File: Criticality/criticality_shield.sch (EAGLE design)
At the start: 20 parts

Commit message: some small improvements
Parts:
- renumbered SV2 to D8-13
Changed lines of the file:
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@@
 <setting verticaltext="up"/>
 </settings>
-<grid distance="0.1" unitdist="inch" unit="inch" style="lines" multiple="1" display="yes" altdistance="0.1" altunitdist="inch" altunit="inch"/>
+<grid distance="0.1" unitdist="inch" unit="inch" style="lines" multiple="1" display="no" altdistance="0.01" altunitdist="inch" altunit="inch"/>
 <layers>
 <layer number="1" name="Top" color="4" fill="1" visible="no" active="no"/>
@@
 <part name="GND2" library="supply1" deviceset="GND" device=""/>
 <part name="D0-7" library="con-lstb" deviceset="MA08-1" device=""/>
-<part name="SV2" library="con-lstb" deviceset="MA08-1" device=""/>
+<part name="D8-13" library="con-lstb" deviceset="MA08-1" device=""/>
 <part name="R9" library="SparkFun-Passives" deviceset="RESISTOR" device="1206" value="100"/>
 <part name="R10" library="SparkFun-Passives" deviceset="RESISTOR" device="1206" value="100"/>
@@
 <instance part="GND2" gate="1" x="-50.8" y="119.38"/>
 <instance part="D0-7" gate="1" x="-88.9" y="111.76" rot="R90"/>
-<instance part="SV2" gate="1" x="-88.9" y="48.26" rot="R90"/>
+<instance part="D8-13" gate="1" x="-88.9" y="48.26" rot="R90"/>
 <instance part="R9" gate="G$1" x="-66.04" y="101.6"/>
 <instance part="R10" gate="G$1" x="-66.04" y="93.98"/>
@@
 <segment>
 <pinref part="R9" gate="G$1" pin="1"/>
-<wire x1="-76.2" y1="101.6" x2="-71.12" y2="101.6" width="0.1524" layer="91"/>
-<junction x="-71.12" y="101.6"/>
-<pinref part="SV2" gate="1" pin="3"/>
+<pinref part="D8-13" gate="1" pin="3"/>
 <wire x1="-86.36" y1="55.88" x2="-71.12" y2="101.6" width="0.1524" layer="91"/>
 <junction x="-86.36" y="55.88"/>
+<junction x="-71.12" y="101.6"/>
 </segment>
 </net>
@@
 <segment>
 <pinref part="R10" gate="G$1" pin="1"/>
-<wire x1="-71.12" y1="93.98" x2="-76.2" y2="93.98" width="0.1524" layer="91"/>
-<junction x="-71.12" y="93.98"/>
-<pinref part="SV2" gate="1" pin="4"/>
+<pinref part="D8-13" gate="1" pin="4"/>
 <wire x1="-88.9" y1="55.88" x2="-71.12" y2="93.98" width="0.1524" layer="91"/>
 <junction x="-88.9" y="55.88"/>
+<junction x="-71.12" y="93.98"/>
 </segment>
 </net>
@@
 <wire x1="-76.2" y1="86.36" x2="-71.12" y2="86.36" width="0.1524" layer="91"/>
 <junction x="-71.12" y="86.36"/>
-<pinref part="SV2" gate="1" pin="5"/>
+<pinref part="D8-13" gate="1" pin="5"/>
 <wire x1="-91.44" y1="55.88" x2="-71.12" y2="86.36" width="0.1524" layer="91"/>
 <junction x="-91.44" y="55.88"/>
@@
 <wire x1="-76.2" y1="78.74" x2="-71.12" y2="78.74" width="0.1524" layer="91"/>
 <junction x="-71.12" y="78.74"/>
-<pinref part="SV2" gate="1" pin="6"/>
+<pinref part="D8-13" gate="1" pin="6"/>
 <wire x1="-93.98" y1="55.88" x2="-71.12" y2="78.74" width="0.1524" layer="91"/>
 <junction x="-93.98" y="55.88"/>
@@
 <wire x1="-76.2" y1="71.12" x2="-71.12" y2="71.12" width="0.1524" layer="91"/>
 <junction x="-71.12" y="71.12"/>
-<pinref part="SV2" gate="1" pin="7"/>
+<pinref part="D8-13" gate="1" pin="7"/>
 <wire x1="-96.52" y1="55.88" x2="-71.12" y2="71.12" width="0.1524" layer="91"/>
 <junction x="-96.52" y="55.88"/>
@@
 <net name="N$15" class="0">
 <segment>
-<pinref part="SV2" gate="1" pin="1"/>
+<pinref part="D8-13" gate="1" pin="1"/>
 <pinref part="R7" gate="G$1" pin="1"/>
 <wire x1="-81.28" y1="55.88" x2="-71.12" y2="116.84" width="0.1524" layer="91"/>
@@
 <net name="N$16" class="0">
 <segment>
-<pinref part="SV2" gate="1" pin="2"/>
+<pinref part="D8-13" gate="1" pin="2"/>
 <pinref part="R8" gate="G$1" pin="1"/>
 <wire x1="-83.82" y1="55.88" x2="-71.12" y2="109.22" width="0.1524" layer="91"/>
@@
 <net name="N$17" class="0">
 <segment>
-<pinref part="SV2" gate="1" pin="8"/>
+<pinref part="D8-13" gate="1" pin="8"/>
 <pinref part="R14" gate="G$1" pin="1"/>
 <wire x1="-99.06" y1="55.88" x2="-71.12" y2="63.5" width="0.1524" layer="91"/>

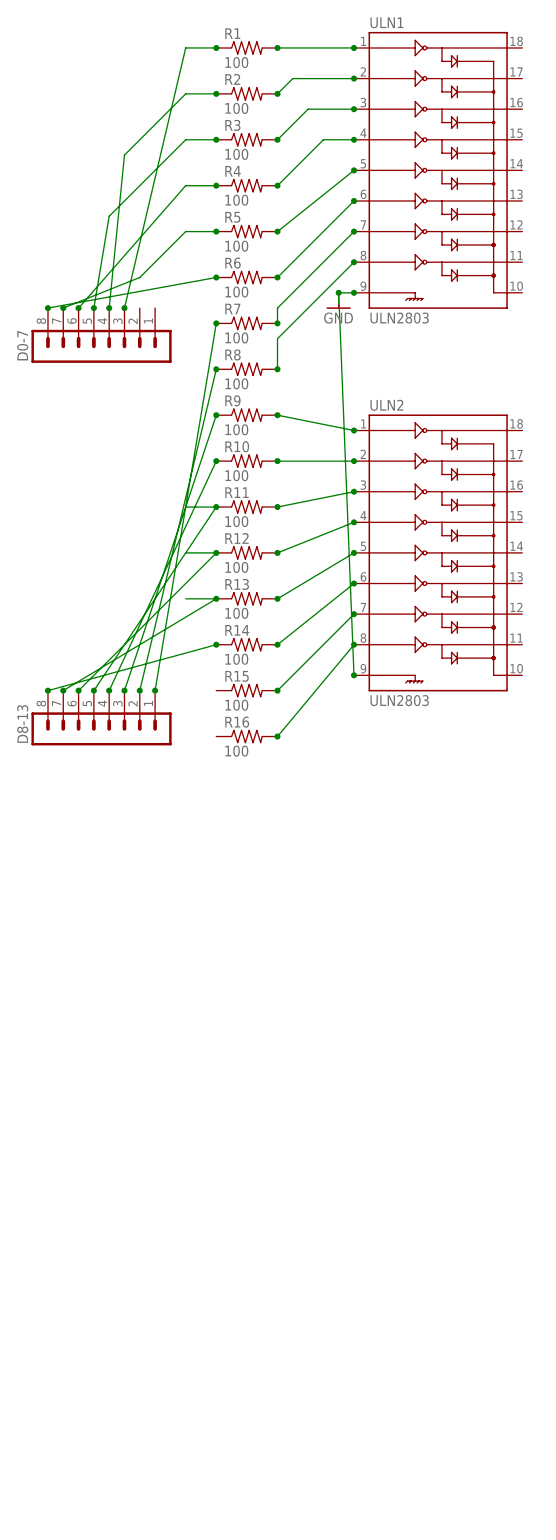
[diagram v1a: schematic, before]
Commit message: added layers to "criticality"
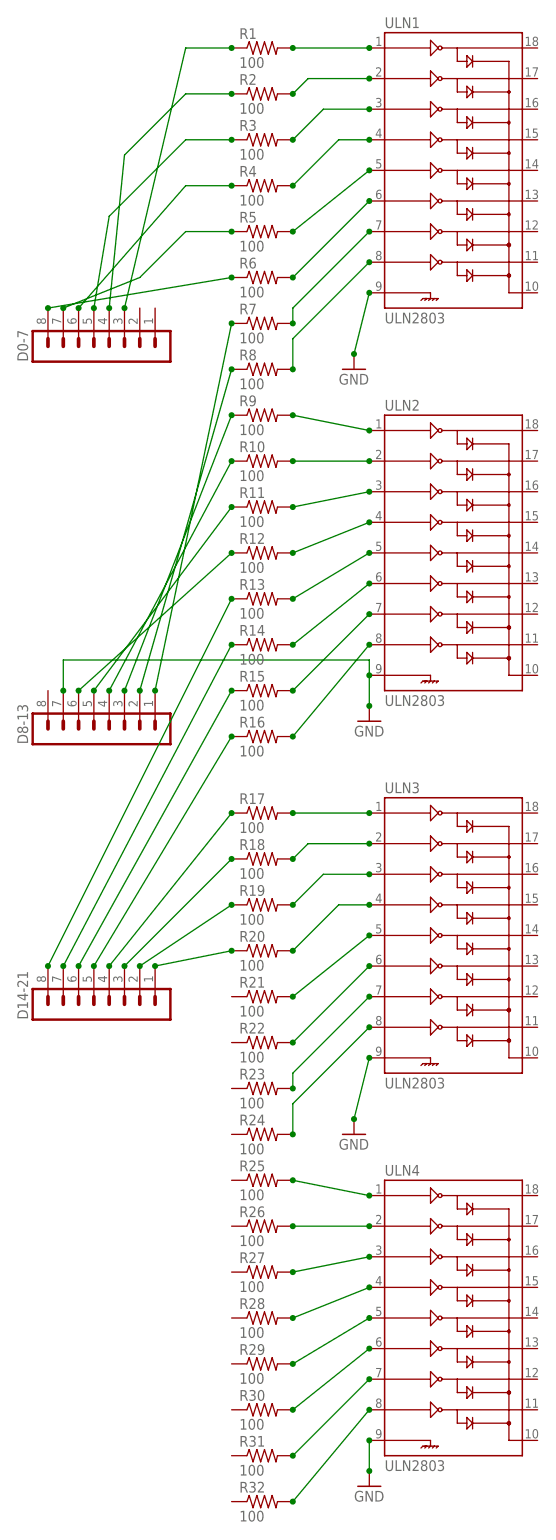
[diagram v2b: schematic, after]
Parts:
- added D14-21: (no value), con-lstb:MA08-1
- added R17, R18, R19, R20, R21, R22, R23, R24, R25, R26, R27, R28, R29, R30, R31, R32: 100, SparkFun-Passives:RESISTOR1206
- added ULN3, ULN4: ULN2803, SparkFun-PowerIC:ULN2803DIP
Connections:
- new net N$31: D14-21.6, R15.1
- new net N$32: D14-21.5, R16.1
- new net N$33: R21.2, ULN3.5
- new net N$34: R22.2, ULN3.6
- new net N$35: R23.2, ULN3.7
- new net N$36: R24.2, ULN3.8
- new net N$37: D14-21.7, R14.1
- new net N$38: D14-21.2, R19.1
- new net N$39: D14-21.1, R20.1
- new net N$40: D14-21.3, R18.1
- new net N$43: R18.2, ULN3.2
- new net N$44: R19.2, ULN3.3
- new net N$45: R20.2, ULN3.4
- new net N$46: R17.2, ULN3.1
- new net N$53: R25.2, ULN4.1
- new net N$54: R26.2, ULN4.2
- new net N$55: R27.2, ULN4.3
- new net N$56: R28.2, ULN4.4
- new net N$57: R29.2, ULN4.5
- new net N$58: R30.2, ULN4.6
- new net N$59: R31.2, ULN4.7
- new net N$60: R32.2, ULN4.8
- net GND: now also D8-13.7, ULN3.9, ULN4.9
- net N$17: now also D14-21.8, R13.1; no longer D8-13.8, R14.1
- net N$23: now also D14-21.4, R17.1; no longer D8-13.7, R13.1
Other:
- moved on the sheet: R1, R10, R11, R12, R13, R14, R15, R16, R2, R3, R4, R5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

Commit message: rearranged, all parts connected
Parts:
- added D22-36_EVEN, D23-37-ODD, D38-52-EVEN, D39-53-ODD: (no value), con-lstb:MA09-1
- added R33, R34, R35, R36, R37, R38, R39, R40, R41, R42, R43, R44, R45, R46, R47, R48: 100, SparkFun-Passives:RESISTOR1206
- added ULN5, ULN6: ULN2803, SparkFun-PowerIC:ULN2803DIP
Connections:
- removed net N$17 (its old number): D14-21.8, R13.1
- new net +5V: D22-36_EVEN.9, D23-37-ODD.9, ULN1.10, ULN2.10, ULN3.10, ULN4.10, ULN5.10, ULN6.10
- new net N$20: D14-21.1, R13.1
- new net N$21: D14-21.2, R14.1
- new net N$22: D14-21.3, R15.1
- new net N$41: D22-36_EVEN.6, R23.1
- new net N$42: D22-36_EVEN.5, R24.1
- new net N$47: D22-36_EVEN.4, R25.1
- new net N$48: D22-36_EVEN.3, R26.1
- new net N$49: D22-36_EVEN.2, R27.1
- new net N$50: D22-36_EVEN.1, R28.1
- new net N$51: D23-37-ODD.8, R29.1
- new net N$52: D23-37-ODD.7, R30.1
- new net N$61: D23-37-ODD.6, R31.1
- new net N$62: D23-37-ODD.5, R32.1
- new net N$63: D23-37-ODD.4, R33.1
- new net N$64: R33.2, ULN5.1
- new net N$65: R34.2, ULN5.2
- new net N$68: R35.2, ULN5.3
- new net N$69: R36.2, ULN5.4
- new net N$70: R37.2, ULN5.5
- new net N$71: R38.2, ULN5.6
- new net N$72: R39.2, ULN5.7
- new net N$73: R40.2, ULN5.8
- new net N$74: R41.2, ULN6.1
- new net N$75: R42.2, ULN6.2
- new net N$76: R43.2, ULN6.3
- new net N$77: R44.2, ULN6.4
- new net N$78: R45.2, ULN6.5
- new net N$79: R46.2, ULN6.6
- new net N$80: R47.2, ULN6.7
- new net N$81: R48.2, ULN6.8
- new net N$82: D23-37-ODD.3, R34.1
- new net N$83: D23-37-ODD.2, R35.1
- new net N$84: D23-37-ODD.1, R36.1
- new net N$85: D38-52-EVEN.9, R37.1
- new net N$86: D38-52-EVEN.8, R38.1
- new net N$87: D38-52-EVEN.7, R39.1
- new net N$88: D38-52-EVEN.6, R40.1
- new net N$89: D38-52-EVEN.5, R41.1
- new net N$90: D38-52-EVEN.4, R42.1
- new net N$91: D38-52-EVEN.3, R43.1
- new net N$92: D38-52-EVEN.2, R44.1
- new net N$93: D39-53-ODD.9, R45.1
- new net N$94: D39-53-ODD.8, R46.1
- new net N$95: D39-53-ODD.7, R47.1
- new net N$96: D39-53-ODD.6, R48.1
- net GND: now also D38-52-EVEN.1, D39-53-ODD.1, ULN5.9, ULN6.9
- net N$23: now also R16.1; no longer R17.1
- net N$31: now also D14-21.5, R17.1; no longer D14-21.6, R15.1
- net N$32: now also D14-21.6, R18.1; no longer D14-21.5, R16.1
- net N$37: now also R19.1; no longer R14.1
- net N$38: now also D14-21.8, R20.1; no longer D14-21.2, R19.1
- net N$39: now also D22-36_EVEN.8, R21.1; no longer D14-21.1, R20.1
- net N$40: now also D22-36_EVEN.7, R22.1; no longer D14-21.3, R18.1
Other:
- note added: "10"
- note added: "11"
- note added: "12"
- note added: "13"
- note added: "14"
- note added: "15"
- note added: "16"
- note added: "17"
- note added: "18"
- note added: "19"
- note added: "2"
- note added: "20"
- note added: "21"
- note added: "22"
- note added: "23"
- note added: "24"
- note added: "25"
- note added: "26"
- note added: "27"
- note added: "28"
- note added: "29"
- note added: "3"
- note added: "30"
- note added: "31"
- note added: "32"
- note added: "33"
- note added: "34"
- note added: "35"
- note added: "36"
- note added: "37"
- note added: "38"
- note added: "39"
- note added: "4"
- note added: "40"
- note added: "41"
- note added: "42"
- note added: "43"
- note added: "44"
- note added: "45"
- note added: "46"
- note added: "47"
- note added: "48"
- note added: "49"
- note added: "5"
- note added: "50"
- note added: "51"
- note added: "52"
- note added: "53"
- note added: "6"
- note added: "7"
- note added: "8"
- note added: "9"
- moved on the sheet: D0-7, D14-21, D8-13

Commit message: clean up, almost finished
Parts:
- removed R1, R10, R11, R12, R13, R14, R15, R16, R17, R18, R19, R2, R20, R21, R22, R23, R24, R25, R26, R27, R28, R29, R3, R30, R31, R32, R33, R34, R35, R36, R37, R38, R39, R4, R40, R41, R42, R43, R44, R45, R46, R47, R48, R5, R6, R7, R8, R9: 100, SparkFun-Passives:RESISTOR1206
- added JP1: (no value), pinhead:PINHD-2X8
- added R-ARRAY-1, R-ARRAY-2, R-ARRAY-3, R-ARRAY-4, R-ARRAY-5, R-ARRAY-6, R-ARRAY-8: (no value), ic-package:DIL16
- added ULN7: ULN2803, SparkFun-PowerIC:ULN2803DIP
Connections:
- new net N$100: R-ARRAY-6.13, ULN6.4
- new net N$101: R-ARRAY-6.12, ULN6.5
- new net N$102: R-ARRAY-6.11, ULN6.6
- new net N$103: R-ARRAY-6.10, ULN6.7
- new net N$104: R-ARRAY-6.9, ULN6.8
- new net N$97: R-ARRAY-6.16, ULN6.1
- new net N$98: R-ARRAY-6.15, ULN6.2
- new net N$99: R-ARRAY-6.14, ULN6.3
- net +5V: now also ULN7.10
- net GND: now also ULN7.9
- net N$1: now also R-ARRAY-8.1; no longer R1.1
- net N$10: now also R-ARRAY-8.15, ULN1.2; no longer R1.2, ULN1.1
- net N$11: now also R-ARRAY-8.14, ULN1.3; no longer R5.2, ULN1.5
- net N$12: now also R-ARRAY-8.13, ULN1.4; no longer R6.2, ULN1.6
- net N$13: now also D8-13.3, R-ARRAY-1.3; no longer R7.2, ULN1.7
- net N$14: now also D8-13.4, R-ARRAY-1.4; no longer R8.2, ULN1.8
- net N$15: now also D8-13.5, R-ARRAY-1.5; no longer D8-13.3, R9.1
- net N$16: now also D8-13.6, R-ARRAY-1.6; no longer D8-13.4, R10.1
- net N$17: now also R-ARRAY-1.16, ULN2.1; no longer D8-13.5, R11.1
- net N$18: now also R-ARRAY-1.15, ULN2.2; no longer R9.2, ULN2.1
- net N$19: now also R-ARRAY-1.14, ULN2.3; no longer D8-13.6, R12.1
- net N$2: now also D0-7.4, R-ARRAY-8.2; no longer D0-7.7, R5.1
- net N$20: now also R-ARRAY-2.1; no longer R13.1
- net N$21: now also R-ARRAY-2.2; no longer R14.1
- net N$22: now also R-ARRAY-2.3; no longer R15.1
- net N$23: now also R-ARRAY-2.4; no longer R16.1
- net N$24: now also R-ARRAY-1.13, ULN2.4; no longer R10.2, ULN2.2
- net N$25: now also R-ARRAY-1.12, ULN2.5; no longer R11.2, ULN2.3
- net N$26: now also R-ARRAY-1.11, ULN2.6; no longer R12.2, ULN2.4
- net N$27: now also D14-21.5, R-ARRAY-2.5; no longer R13.2, ULN2.5
- net N$28: now also D14-21.6, R-ARRAY-2.6; no longer R14.2, ULN2.6
- net N$29: now also D14-21.7, R-ARRAY-2.7; no longer R15.2, ULN2.7
- net N$3: now also D0-7.5, R-ARRAY-8.3; no longer D0-7.8, R6.1
- net N$30: now also D14-21.8, R-ARRAY-2.8; no longer R16.2, ULN2.8
- net N$31: now also R-ARRAY-2.16, ULN3.1; no longer D14-21.5, R17.1
- net N$32: now also R-ARRAY-2.15, ULN3.2; no longer D14-21.6, R18.1
- net N$33: now also R-ARRAY-2.14, ULN3.3; no longer R21.2, ULN3.5
- net N$34: now also R-ARRAY-2.13, ULN3.4; no longer R22.2, ULN3.6
- net N$35: now also D22-36_EVEN.1, R-ARRAY-3.1; no longer R23.2, ULN3.7
- net N$36: now also D22-36_EVEN.2, R-ARRAY-3.2; no longer R24.2, ULN3.8
- net N$37: now also R-ARRAY-2.12, ULN3.5; no longer D14-21.7, R19.1
- net N$38: now also R-ARRAY-2.11, ULN3.6; no longer D14-21.8, R20.1
- net N$39: now also D22-36_EVEN.3, R-ARRAY-3.3; no longer D22-36_EVEN.8, R21.1
- net N$4: now also R-ARRAY-8.4; no longer R4.1
- net N$40: now also D22-36_EVEN.4, R-ARRAY-3.4; no longer D22-36_EVEN.7, R22.1
- net N$41: now also D22-36_EVEN.5, R-ARRAY-3.5; no longer D22-36_EVEN.6, R23.1
- net N$42: now also D22-36_EVEN.6, R-ARRAY-3.6; no longer D22-36_EVEN.5, R24.1
- net N$43: now also R-ARRAY-2.10, ULN3.7; no longer R18.2, ULN3.2
- net N$44: now also R-ARRAY-2.9, ULN3.8; no longer R19.2, ULN3.3
- net N$45: now also D22-36_EVEN.7, R-ARRAY-3.7; no longer R20.2, ULN3.4
- net N$46: now also D22-36_EVEN.8, R-ARRAY-3.8; no longer R17.2, ULN3.1
- net N$47: now also R-ARRAY-3.16, ULN4.1; no longer D22-36_EVEN.4, R25.1
- net N$48: now also R-ARRAY-3.15, ULN4.2; no longer D22-36_EVEN.3, R26.1
- net N$49: now also R-ARRAY-3.14, ULN4.3; no longer D22-36_EVEN.2, R27.1
- net N$5: now also R-ARRAY-1.1; no longer R7.1
- net N$50: now also R-ARRAY-3.13, ULN4.4; no longer D22-36_EVEN.1, R28.1
- net N$51: now also R-ARRAY-4.1; no longer R29.1
- net N$52: now also R-ARRAY-4.2; no longer R30.1
- net N$53: now also R-ARRAY-3.12, ULN4.5; no longer R25.2, ULN4.1
- net N$54: now also R-ARRAY-3.11, ULN4.6; no longer R26.2, ULN4.2
- net N$55: now also R-ARRAY-3.10, ULN4.7; no longer R27.2, ULN4.3
- net N$56: now also R-ARRAY-3.9, ULN4.8; no longer R28.2, ULN4.4
- net N$57: now also D23-37-ODD.6, R-ARRAY-4.3; no longer R29.2, ULN4.5
- net N$58: now also D23-37-ODD.5, R-ARRAY-4.4; no longer R30.2, ULN4.6
- net N$59: now also D23-37-ODD.4, R-ARRAY-4.5; no longer R31.2, ULN4.7
- net N$6: now also R-ARRAY-1.2; no longer R8.1
- net N$60: now also D23-37-ODD.3, R-ARRAY-4.6; no longer R32.2, ULN4.8
- net N$61: now also D23-37-ODD.2, R-ARRAY-4.7; no longer D23-37-ODD.6, R31.1
- net N$62: now also D23-37-ODD.1, R-ARRAY-4.8; no longer D23-37-ODD.5, R32.1
- net N$63: now also R-ARRAY-4.16, ULN7.1; no longer D23-37-ODD.4, R33.1
- net N$64: now also R-ARRAY-4.15, ULN7.2; no longer R33.2, ULN5.1
- net N$65: now also R-ARRAY-4.14, ULN7.3; no longer R34.2, ULN5.2
- net N$66: now also R-ARRAY-8.12, ULN1.5; no longer D0-7.5, R3.1
- net N$67: now also R-ARRAY-8.11, ULN1.6; no longer D0-7.4, R2.1
- net N$68: now also R-ARRAY-4.13, ULN7.4; no longer R35.2, ULN5.3
- net N$69: now also R-ARRAY-4.12, ULN7.5; no longer R36.2, ULN5.4
- net N$7: now also D0-7.7, R-ARRAY-8.5; no longer R2.2, ULN1.2
- net N$70: now also D38-52-EVEN.2, R-ARRAY-5.1; no longer R37.2, ULN5.5
- net N$71: now also D38-52-EVEN.3, R-ARRAY-5.2; no longer R38.2, ULN5.6
- net N$72: now also D38-52-EVEN.4, R-ARRAY-5.3; no longer R39.2, ULN5.7
- net N$73: now also D38-52-EVEN.5, R-ARRAY-5.4; no longer R40.2, ULN5.8
- net N$74: now also D38-52-EVEN.6, R-ARRAY-5.5; no longer R41.2, ULN6.1
- net N$75: now also D38-52-EVEN.7, R-ARRAY-5.6; no longer R42.2, ULN6.2
- net N$76: now also D38-52-EVEN.8, R-ARRAY-5.7; no longer R43.2, ULN6.3
- net N$77: now also D38-52-EVEN.9, R-ARRAY-5.8; no longer R44.2, ULN6.4
- net N$78: now also R-ARRAY-5.16, ULN5.1; no longer R45.2, ULN6.5
- net N$79: now also R-ARRAY-5.15, ULN5.2; no longer R46.2, ULN6.6
- net N$8: now also D0-7.8, R-ARRAY-8.6; no longer R3.2, ULN1.3
- net N$80: now also R-ARRAY-5.14, ULN5.3; no longer R47.2, ULN6.7
- net N$81: now also R-ARRAY-5.13, ULN5.4; no longer R48.2, ULN6.8
- net N$82: now also R-ARRAY-4.11, ULN7.6; no longer D23-37-ODD.3, R34.1
- net N$83: now also R-ARRAY-4.10, ULN7.7; no longer D23-37-ODD.2, R35.1
- net N$84: now also R-ARRAY-4.9, ULN7.8; no longer D23-37-ODD.1, R36.1
- net N$85: now also R-ARRAY-5.12, ULN5.5; no longer D38-52-EVEN.9, R37.1
- net N$86: now also R-ARRAY-5.11, ULN5.6; no longer D38-52-EVEN.8, R38.1
- net N$87: now also R-ARRAY-5.10, ULN5.7; no longer D38-52-EVEN.7, R39.1
- net N$88: now also R-ARRAY-5.9, ULN5.8; no longer D38-52-EVEN.6, R40.1
- net N$89: now also D39-53-ODD.9, R-ARRAY-6.1; no longer D38-52-EVEN.5, R41.1
- net N$9: now also R-ARRAY-8.16, ULN1.1; no longer R4.2, ULN1.4
- net N$90: now also D39-53-ODD.8, R-ARRAY-6.2; no longer D38-52-EVEN.4, R42.1
- net N$91: now also D39-53-ODD.7, R-ARRAY-6.3; no longer D38-52-EVEN.3, R43.1
- net N$92: now also D39-53-ODD.6, R-ARRAY-6.4; no longer D38-52-EVEN.2, R44.1
- net N$93: now also D39-53-ODD.5, R-ARRAY-6.5; no longer D39-53-ODD.9, R45.1
- net N$94: now also D39-53-ODD.4, R-ARRAY-6.6; no longer D39-53-ODD.8, R46.1
- net N$95: now also D39-53-ODD.3, R-ARRAY-6.7; no longer D39-53-ODD.7, R47.1
- net N$96: now also D39-53-ODD.2, R-ARRAY-6.8; no longer D39-53-ODD.6, R48.1
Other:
- moved on the sheet: D0-7, D22-36_EVEN, D38-52-EVEN, D8-13, ULN1, ULN2, ULN3, ULN4, ULN5

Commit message: before autoroute, fitted to mega
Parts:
- added JP2, JP3, JP4, JP5, JP6, JP7: (no value), pinhead:PINHD-2X8
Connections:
- new net N$105: JP1.1, ULN1.18
- new net N$106: JP1.3, ULN1.17
- new net N$107: JP1.5, ULN1.16
- new net N$108: JP1.7, ULN1.15
- new net N$109: JP1.9, ULN1.14
- new net N$110: JP1.11, ULN1.13
- new net N$111: JP1.13
- new net N$112: JP1.15
- new net N$113: JP4.1, ULN4.18
- new net N$114: JP4.3, ULN4.17
- new net N$115: JP4.5, ULN4.16
- new net N$116: JP4.7, ULN4.15
- new net N$117: JP4.9, ULN4.14
- new net N$118: JP4.11, ULN4.13
- new net N$119: JP4.13, ULN4.12
- new net N$120: JP4.15, ULN4.11
- new net N$121: JP2.1, ULN2.18
- new net N$122: JP2.3, ULN2.17
- new net N$123: JP2.5, ULN2.16
- new net N$124: JP2.7, ULN2.15
- new net N$125: JP2.9, ULN2.14
- new net N$126: JP2.11, ULN2.13
- new net N$127: JP3.1, ULN3.18
- new net N$128: JP3.3, ULN3.17
- new net N$129: JP3.5, ULN3.16
- new net N$130: JP3.7, ULN3.15
- new net N$131: JP3.9, ULN3.14
- new net N$132: JP3.11, ULN3.13
- new net N$133: JP3.13, ULN3.12
- new net N$134: JP3.15, ULN3.11
- new net N$135: JP6.1, ULN5.18
- new net N$136: JP6.3, ULN5.17
- new net N$137: JP6.5, ULN5.16
- new net N$138: JP6.7, ULN5.15
- new net N$139: JP6.9, ULN5.14
- new net N$140: JP6.11, ULN5.13
- new net N$141: JP6.13, ULN5.12
- new net N$142: JP6.15, ULN5.11
- new net N$143: JP5.15, ULN7.11
- new net N$144: JP5.13, ULN7.12
- new net N$145: JP5.11, ULN7.13
- new net N$146: JP5.9, ULN7.14
- new net N$147: JP5.7, ULN7.15
- new net N$148: JP5.5, ULN7.16
- new net N$149: JP5.3, ULN7.17
- new net N$150: JP5.1, ULN7.18
- new net N$151: JP7.1, ULN6.18
- new net N$152: JP7.3, ULN6.17
- new net N$153: JP7.5, ULN6.16
- new net N$154: JP7.7, ULN6.15
- new net N$155: JP7.9, ULN6.14
- new net N$156: JP7.11, ULN6.13
- new net N$157: JP7.13, ULN6.12
- new net N$158: JP7.15, ULN6.11
- net +5V: now also JP1.10, JP1.12, JP1.14, JP1.16, JP1.2, JP1.4, JP1.6, JP1.8, JP2.10, JP2.12, JP2.14, JP2.16, JP2.2, JP2.4, JP2.6, JP2.8, JP3.10, JP3.12, JP3.14, JP3.16, JP3.2, JP3.4, JP3.6, JP3.8, JP4.10, JP4.12, JP4.14, JP4.16, JP4.2, JP4.4, JP4.6, JP4.8, JP5.10, JP5.12, JP5.14, JP5.16, JP5.2, JP5.4, JP5.6, JP5.8, JP6.10, JP6.12, JP6.14, JP6.16, JP6.2, JP6.4, JP6.6, JP6.8, JP7.10, JP7.12, JP7.14, JP7.16, JP7.2, JP7.4, JP7.6, JP7.8
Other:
- moved on the sheet: D14-21, D22-36_EVEN, D23-37-ODD, D38-52-EVEN, D39-53-ODD, R-ARRAY-2, R-ARRAY-3, R-ARRAY-4, R-ARRAY-5, R-ARRAY-6, ULN3, ULN4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
